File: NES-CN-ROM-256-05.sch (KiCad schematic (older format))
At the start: 15 parts, among them U1 CIC 6113, U2 74HC161, U3 ATtiny13A-PU, U4 CHR-ROM, U5 PRG-ROM

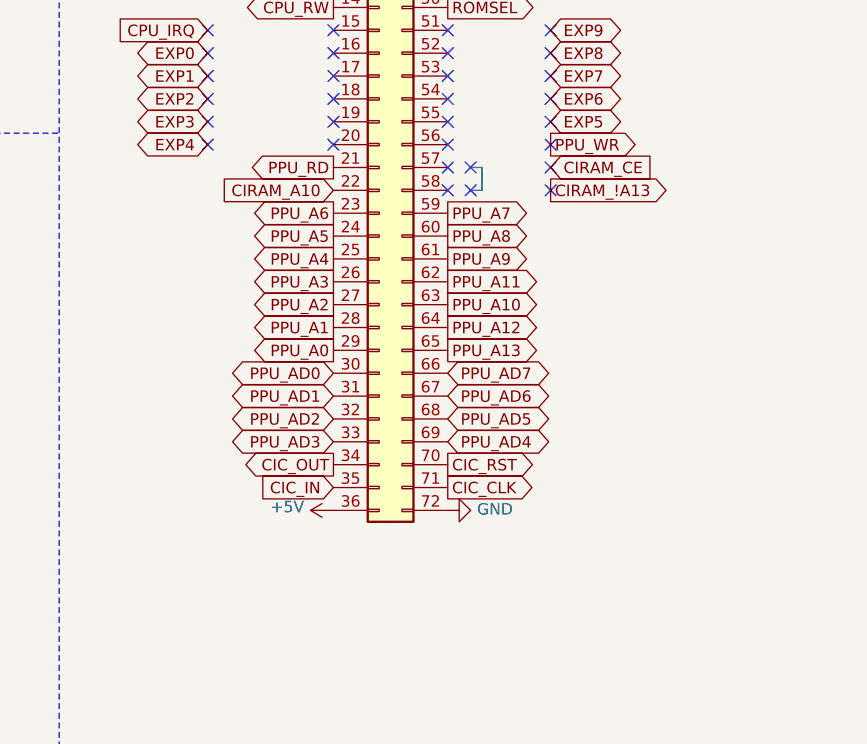
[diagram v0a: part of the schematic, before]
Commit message: [1] Connect cartridge pins 57-58 for NES internal VRAM enable line. [2] Regenerate gerbers.
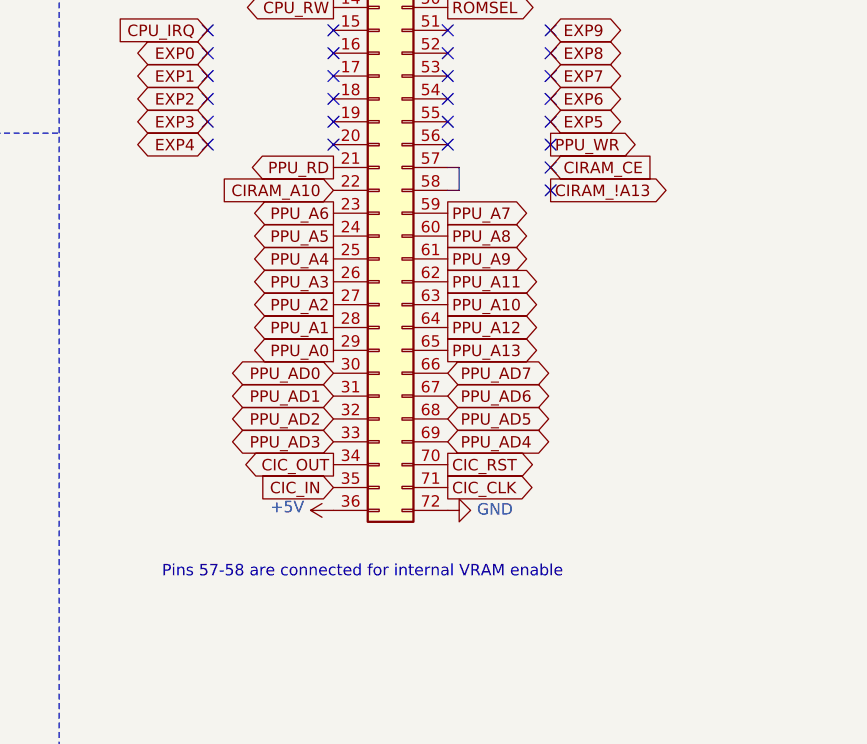
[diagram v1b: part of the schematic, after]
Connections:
- net at EDGE1.57 (Pin_57): now also EDGE1.58 (Pin_58)
- no-connect marks 40 -> 36
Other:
- note added: "Pins 57-58 are connected for internal VRAM enable"
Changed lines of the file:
@@
 Sheet 1 1
 Title "NES-CN-ROM-256-05 Schematic"
-Date "2022-04-25"
-Rev "v01"
+Date "2022-06-09"
+Rev "v01.1"
 Comp ""
 Comment1 "License: https://creativecommons.org/licenses/by-sa/4.0/"
@@
 Text GLabel 2950 7050 0    50   Input ~ 0
 PPU_A11
-NoConn ~ 10000 3700
-NoConn ~ 10000 3800
-NoConn ~ 10100 3700
-NoConn ~ 10100 3800
-Wire Wire Line
-	10100 3700 10150 3700
-Wire Wire Line
-	10150 3700 10150 3800
-Wire Wire Line
-	10150 3800 10100 3800
+Wire Wire Line
+	10000 3700 10050 3700
+Wire Wire Line
+	10050 3700 10050 3800
+Wire Wire Line
+	10050 3800 10000 3800
+Text Notes 8750 5500 0    50   ~ 0
+Pins 57-58 are connected for internal VRAM enable
 $EndSCHEMATC

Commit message: New board layout to support 32 dip flash chips
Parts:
- U4, U5: footprint Package_DIP:DIP-28_W15.24mm -> Package_DIP:DIP-32_W15.24mm; symbol Memory_EPROM:27C512 -> Memory_Flash:SST39SF040
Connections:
- net +5V: now also U4.2 (A16), U4.3 (A15), U4.30 (A17), U4.31 (PGM), U4.32 (VCC), U5.2 (A16), U5.3 (A15), U5.30 (A17), U5.31 (PGM), U5.32 (VCC); no longer U4.28 (VCC), U5.28 (VCC)
- net CHR_A13: now also U4.28 (A13); no longer U4.26 (A13)
- net CHR_A14: now also U4.29 (A14); no longer U4.27 (A14)
- net CPU_A0: now also U5.12 (A0); no longer U5.10 (A0)
- net CPU_A1: now also U5.11 (A1); no longer U5.9 (A1)
- net CPU_A10: now also U5.23 (A10); no longer U5.21 (A10)
- net CPU_A11: now also U5.25 (A11); no longer U5.23 (A11)
- net CPU_A12: now also U5.4 (A12); no longer U5.2 (A12)
- net CPU_A13: now also U5.28 (A13); no longer U5.26 (A13)
- net CPU_A2: now also U5.10 (A2); no longer U5.8 (A2)
- net CPU_A3: now also U5.9 (A3); no longer U5.7 (A3)
- net CPU_A4: now also U5.8 (A4); no longer U5.6 (A4)
- net CPU_A5: now also U5.7 (A5); no longer U5.5 (A5)
- net CPU_A6: now also U5.6 (A6); no longer U5.4 (A6)
- net CPU_A7: now also U5.5 (A7); no longer U5.3 (A7)
- net CPU_A8: now also U5.27 (A8); no longer U5.25 (A8)
- net CPU_A9: now also U5.26 (A9); no longer U5.24 (A9)
- net CPU_D0: now also U5.13 (D0); no longer U5.11 (D0)
- net CPU_D1: now also U5.14 (D1); no longer U5.12 (D1)
- net CPU_D2: now also U5.15 (D2); no longer U5.13 (D2)
- net CPU_D3: now also U5.17 (D3); no longer U5.15 (D3)
- net CPU_D4: now also U5.18 (D4); no longer U5.16 (D4)
- net CPU_D5: now also U5.19 (D5); no longer U5.17 (D5)
- net CPU_D6: now also U5.20 (D6); no longer U5.18 (D6)
- net CPU_D7: now also U5.21 (D7); no longer U5.19 (D7)
- net GND: now also U4.16 (GND), U5.16 (GND), U5.22 (CE); no longer U4.14 (GND), U5.14 (GND), U5.20 (~CE)
- net PPU_A0: now also U4.12 (A0); no longer U4.10 (A0)
- net PPU_A1: now also U4.11 (A1); no longer U4.9 (A1)
- net PPU_A10: now also U4.23 (A10); no longer U4.21 (A10)
- net PPU_A11: now also U4.25 (A11); no longer U4.23 (A11)
- net PPU_A12: now also U4.4 (A12); no longer U4.2 (A12)
- net PPU_A13: now also U4.22 (CE); no longer U4.20 (~CE)
- net PPU_A2: now also U4.10 (A2); no longer U4.8 (A2)
- net PPU_A3: now also U4.9 (A3); no longer U4.7 (A3)
- net PPU_A4: now also U4.8 (A4); no longer U4.6 (A4)
- net PPU_A5: now also U4.7 (A5); no longer U4.5 (A5)
- net PPU_A6: now also U4.6 (A6); no longer U4.4 (A6)
- net PPU_A7: now also U4.5 (A7); no longer U4.3 (A7)
- net PPU_A8: now also U4.27 (A8); no longer U4.25 (A8)
- net PPU_A9: now also U4.26 (A9); no longer U4.24 (A9)
- net PPU_AD0: now also U4.13 (D0); no longer U4.11 (D0)
- net PPU_AD1: now also U4.14 (D1); no longer U4.12 (D1)
- net PPU_AD2: now also U4.15 (D2); no longer U4.13 (D2)
- net PPU_AD3: now also U4.17 (D3); no longer U4.15 (D3)
- net PPU_AD4: now also U4.18 (D4); no longer U4.16 (D4)
- net PPU_AD5: now also U4.19 (D5); no longer U4.17 (D5)
- net PPU_AD6: now also U4.20 (D6); no longer U4.18 (D6)
- net PPU_AD7: now also U4.21 (D7); no longer U4.19 (D7)
- net PPU_RD: now also U4.24 (OE); no longer U4.22 (~OE)
- net PRG_A14: now also U5.29 (A14); no longer U5.27 (A14)
- net ROMSEL: now also U5.24 (OE); no longer U5.22 (~OE)
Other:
- note added: "CHR ROM (SST39SF0x0A support)"
- note added: "PRG ROM (SST39SF0x0A support)"
- note added: "Upper address lines unused\nNES sees high 32KB"
- note removed: "CHR ROM"
- note removed: "PRG ROM"
